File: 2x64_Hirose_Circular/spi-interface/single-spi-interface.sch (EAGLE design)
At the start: 52 parts, among them P0 BLUE, P1 BLUE, P2 BLUE, P3 BLUE, P4 BLUE, Q1 SSM3K324, Q2 SSM3J328

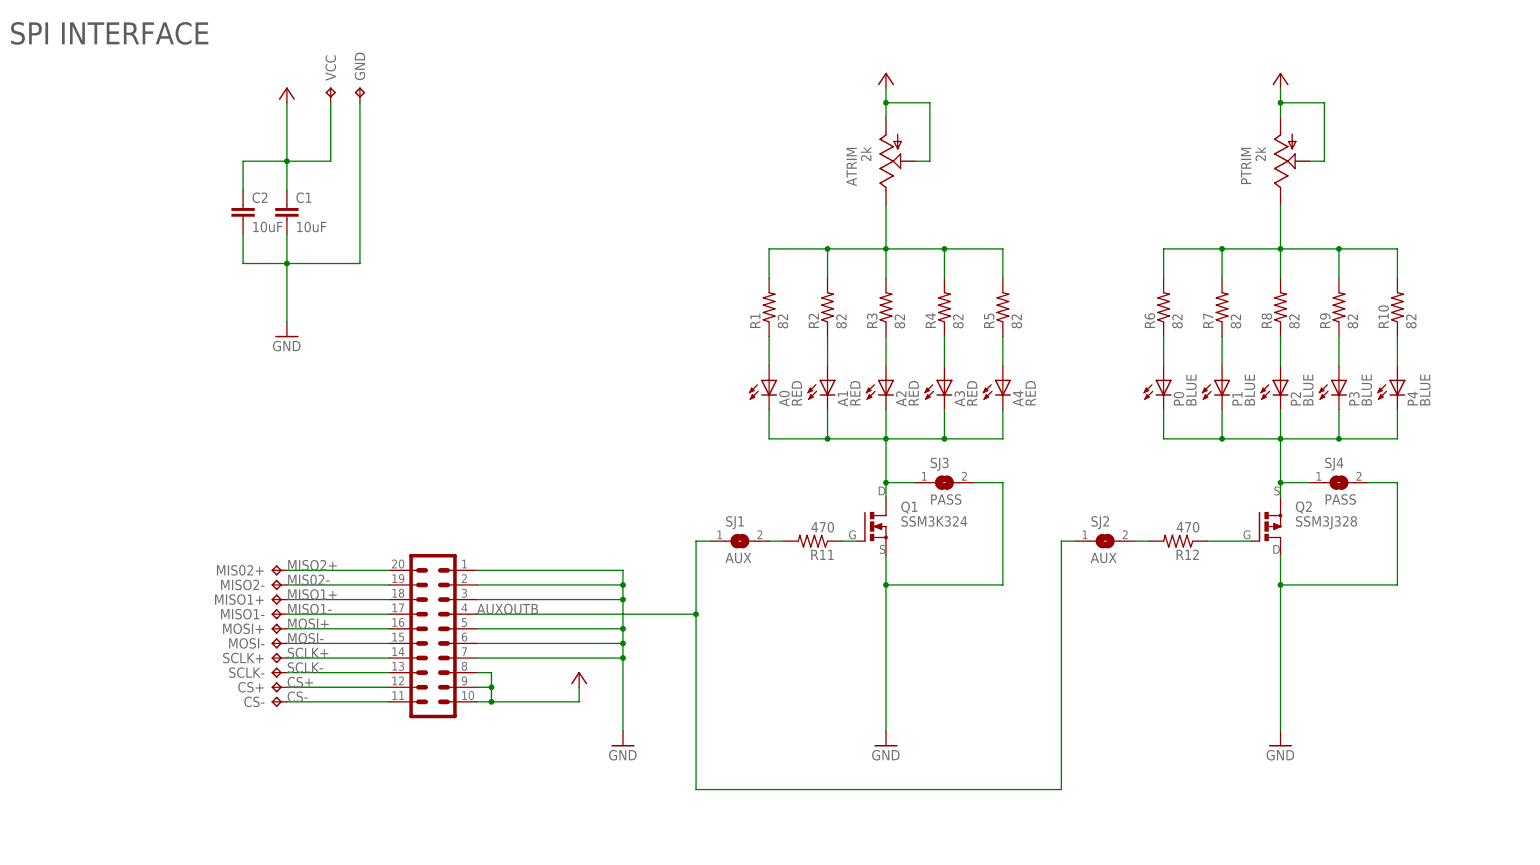
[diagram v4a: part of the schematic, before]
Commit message: Started applying revisions obtained from mechanical mockups
- This is the start of work toward rev 1.1 of Hirose 128 headstages.
- Headstages are designed to be semi-perminent. They are travel with the
  animal until it is sacraficed.
- Major changes to SPI interface board to get it working with Oat
  tracker and to conform with the semi-periment design decision.
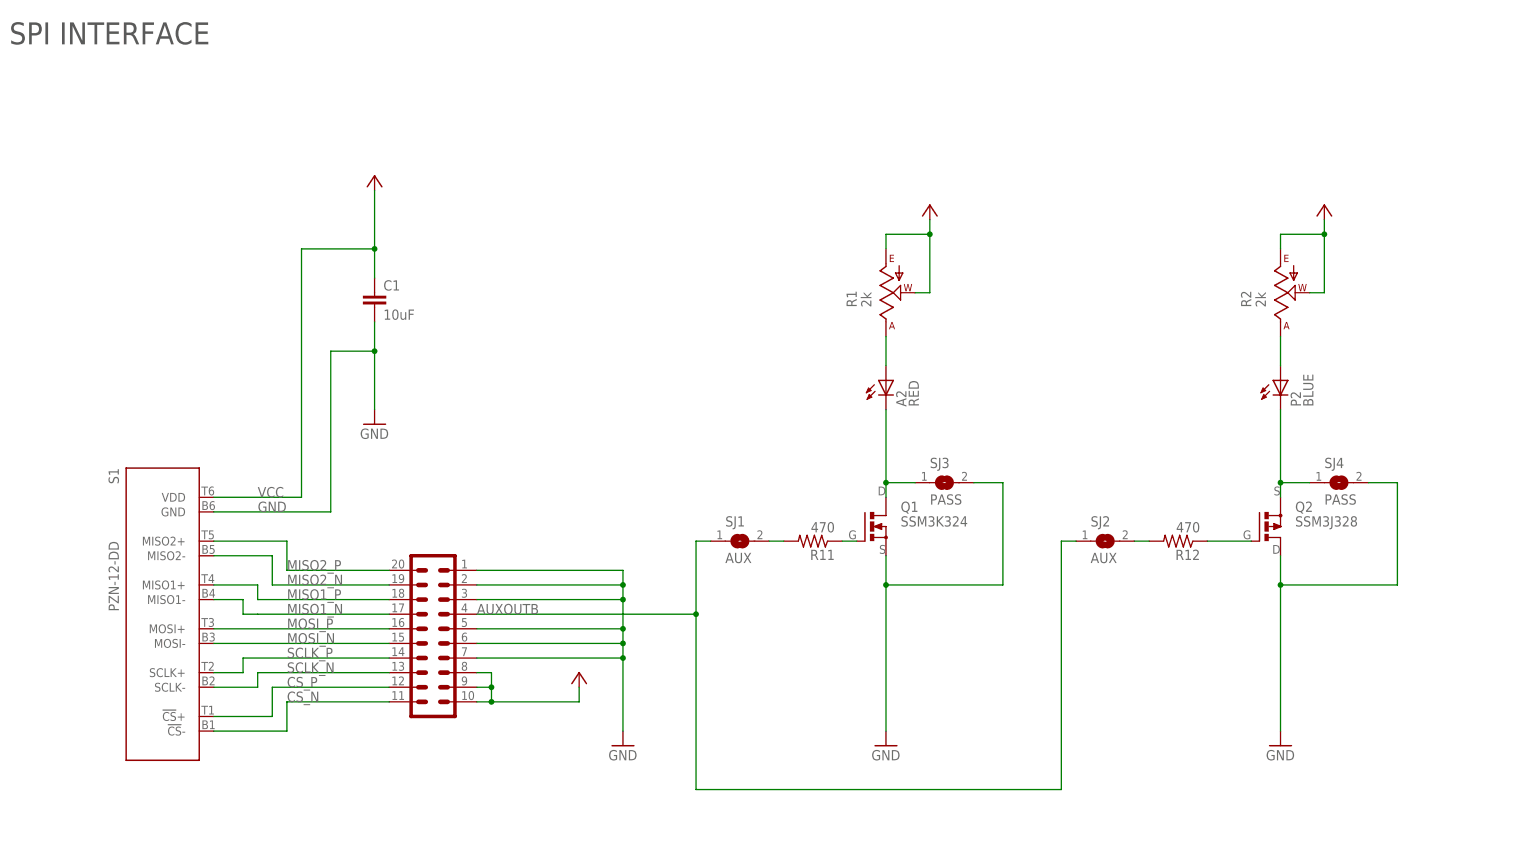
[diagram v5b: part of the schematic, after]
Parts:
- removed A0, A1, A3, A4: RED, jonnew:LED_0402
- removed ATRIM, PTRIM: 2k, headstage:TRIM_EIA/EIAJ
- removed C2: 10uF, headstage:C_0805
- removed CS+, MIS02+, MISO1+, MOSI+, SCLK+, VCC: TP_SPI_WIRE+, jonnew:TP_SPI_WIRE+
- removed CS-, GND, MISO1-, MISO2-, MOSI-, SCLK-: TP_SPI_WIRE-, jonnew:TP_SPI_WIRE-
- removed P0, P1, P3, P4: BLUE, jonnew:LED_0402
- removed R10, R3, R4, R5, R6, R7, R8, R9: 82, jonnew:R_0402
- added S1: PZN-12-DD, jonnew:RHD2000-CABLE-AMP-SIDE_PZN-12-DD
- A2, P2: device jonnew:LED_0402 -> jonnew:LED_MLE
- R1, R2: value 82 -> 2k; device jonnew:R_0402 -> jonnew:TRIM_US-SM-42/43W
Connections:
- removed net CS+: CS+.TP, DIO_E1B.12
- removed net CS-: CS-.TP, DIO_E1B.11
- removed net MIS02-: DIO_E1B.19, MISO2-.TP
- removed net MISO1+: DIO_E1B.18, MISO1+.TP
- removed net MISO1-: DIO_E1B.17, MISO1-.TP
- removed net MISO2+: DIO_E1B.20, MIS02+.TP
- removed net MOSI+: DIO_E1B.16, MOSI+.TP
- removed net MOSI-: DIO_E1B.15, MOSI-.TP
- removed net N$1: ATRIM.E, R1.2, R2.2, R3.2, R4.2, R5.2
- removed net N$10: A3.A, R4.1
- removed net N$11: P3.A, R9.1
- removed net N$12: P1.A, R7.1
- removed net N$14: A4.A, R5.1
- removed net N$15: P4.A, R10.1
- removed net N$2: P0.A, R6.1
- removed net N$3: A0.A, R1.1
- removed net N$6: PTRIM.E, R10.2, R6.2, R7.2, R8.2, R9.2
- removed net N$8: A1.A, R2.1
- removed net SCLK+: DIO_E1B.14, SCLK+.TP
- removed net SCLK-: DIO_E1B.13, SCLK-.TP
- new net CS_N: DIO_E1B.11, S1.!CS!-
- new net CS_P: DIO_E1B.12, S1.!CS!+
- new net MISO1_N: DIO_E1B.17, S1.MISO1-
- new net MISO1_P: DIO_E1B.18, S1.MISO1+
- new net MISO2_N: DIO_E1B.19, S1.MISO2-
- new net MISO2_P: DIO_E1B.20, S1.MISO2+
- new net MOSI_N: DIO_E1B.15, S1.MOSI-
- new net MOSI_P: DIO_E1B.16, S1.MOSI+
- new net SCLK_N: DIO_E1B.13, S1.SCLK-
- new net SCLK_P: DIO_E1B.14, S1.SCLK+
- net B2: no longer P0.C, P1.C, P3.C, P4.C
- net F1: no longer A0.C, A1.C, A3.C, A4.C
- net GND: now also S1.GND; no longer C2.2, GND.TP
- net N$13: now also R2.A; no longer R8.1
- net N$9: now also R1.A; no longer R3.1
- net VCC: now also R1.E, R1.W, R2.E, R2.W, S1.VDD; no longer ATRIM.A, ATRIM.S, C2.1, PTRIM.A, PTRIM.S, VCC.TP
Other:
- moved on the sheet: C1

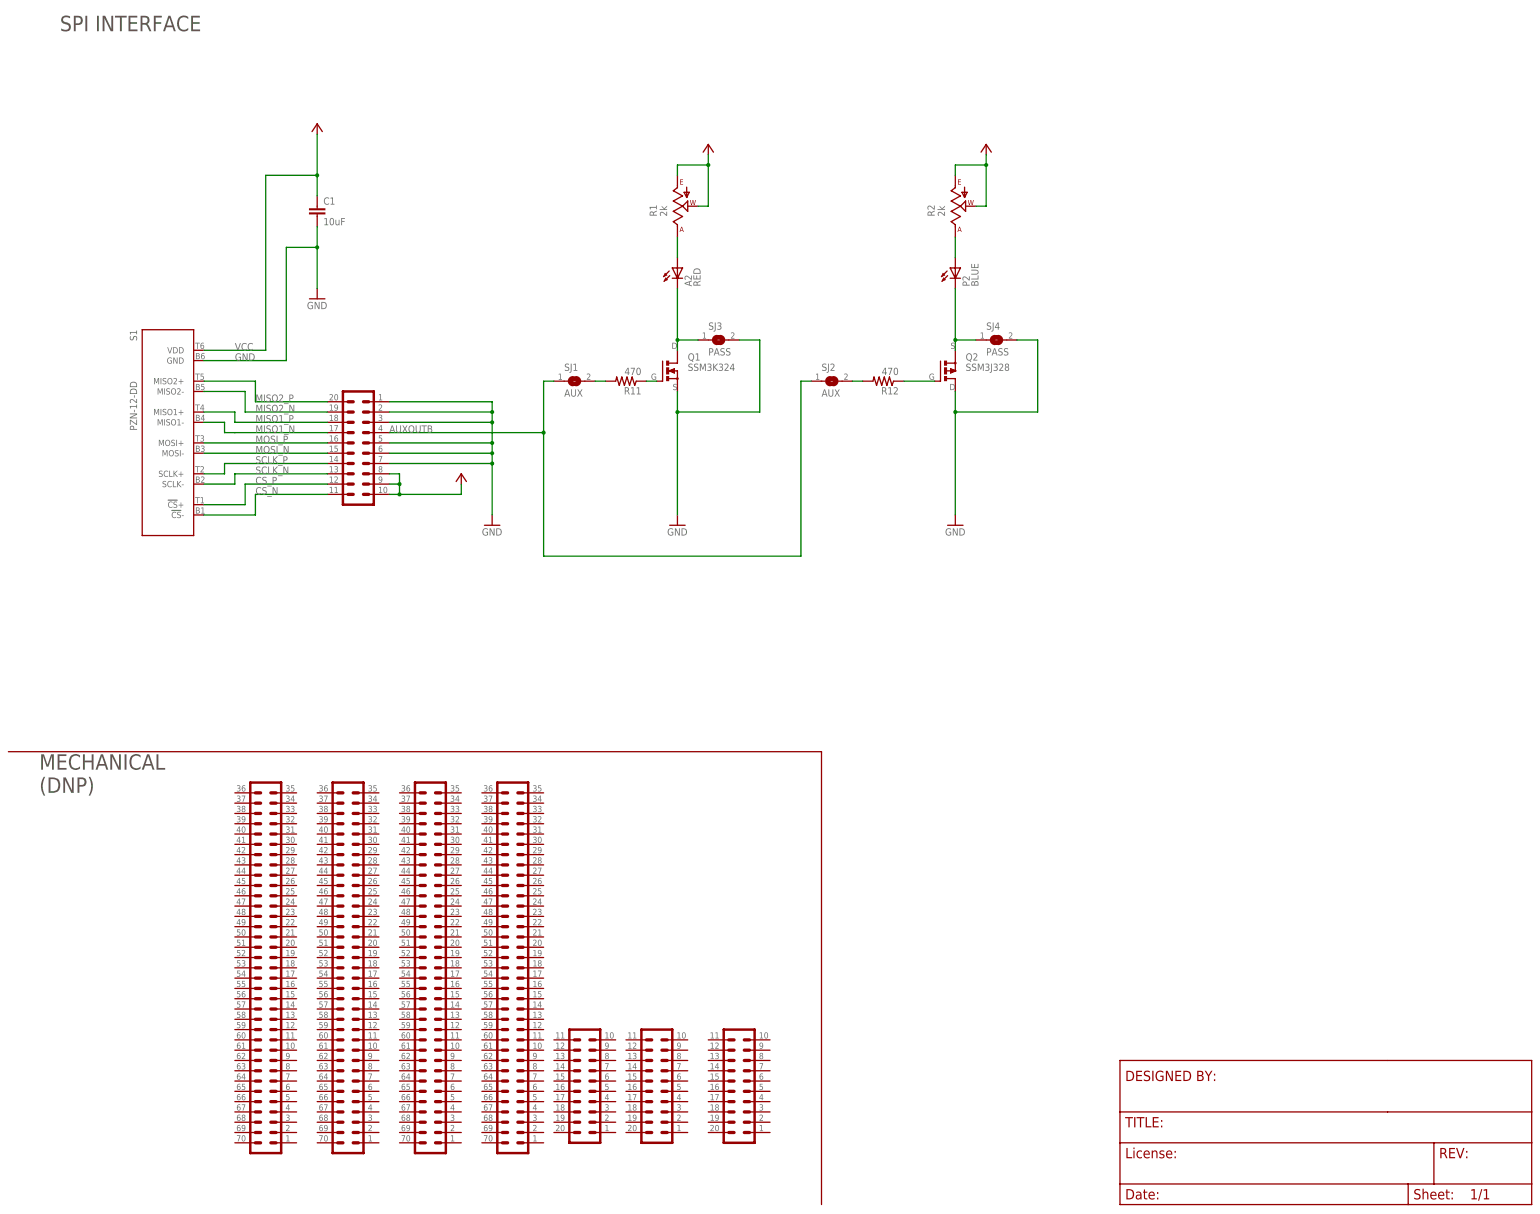
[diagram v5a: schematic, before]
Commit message: Nearly finished with revision 1.1 of Hirose-128 headstage.
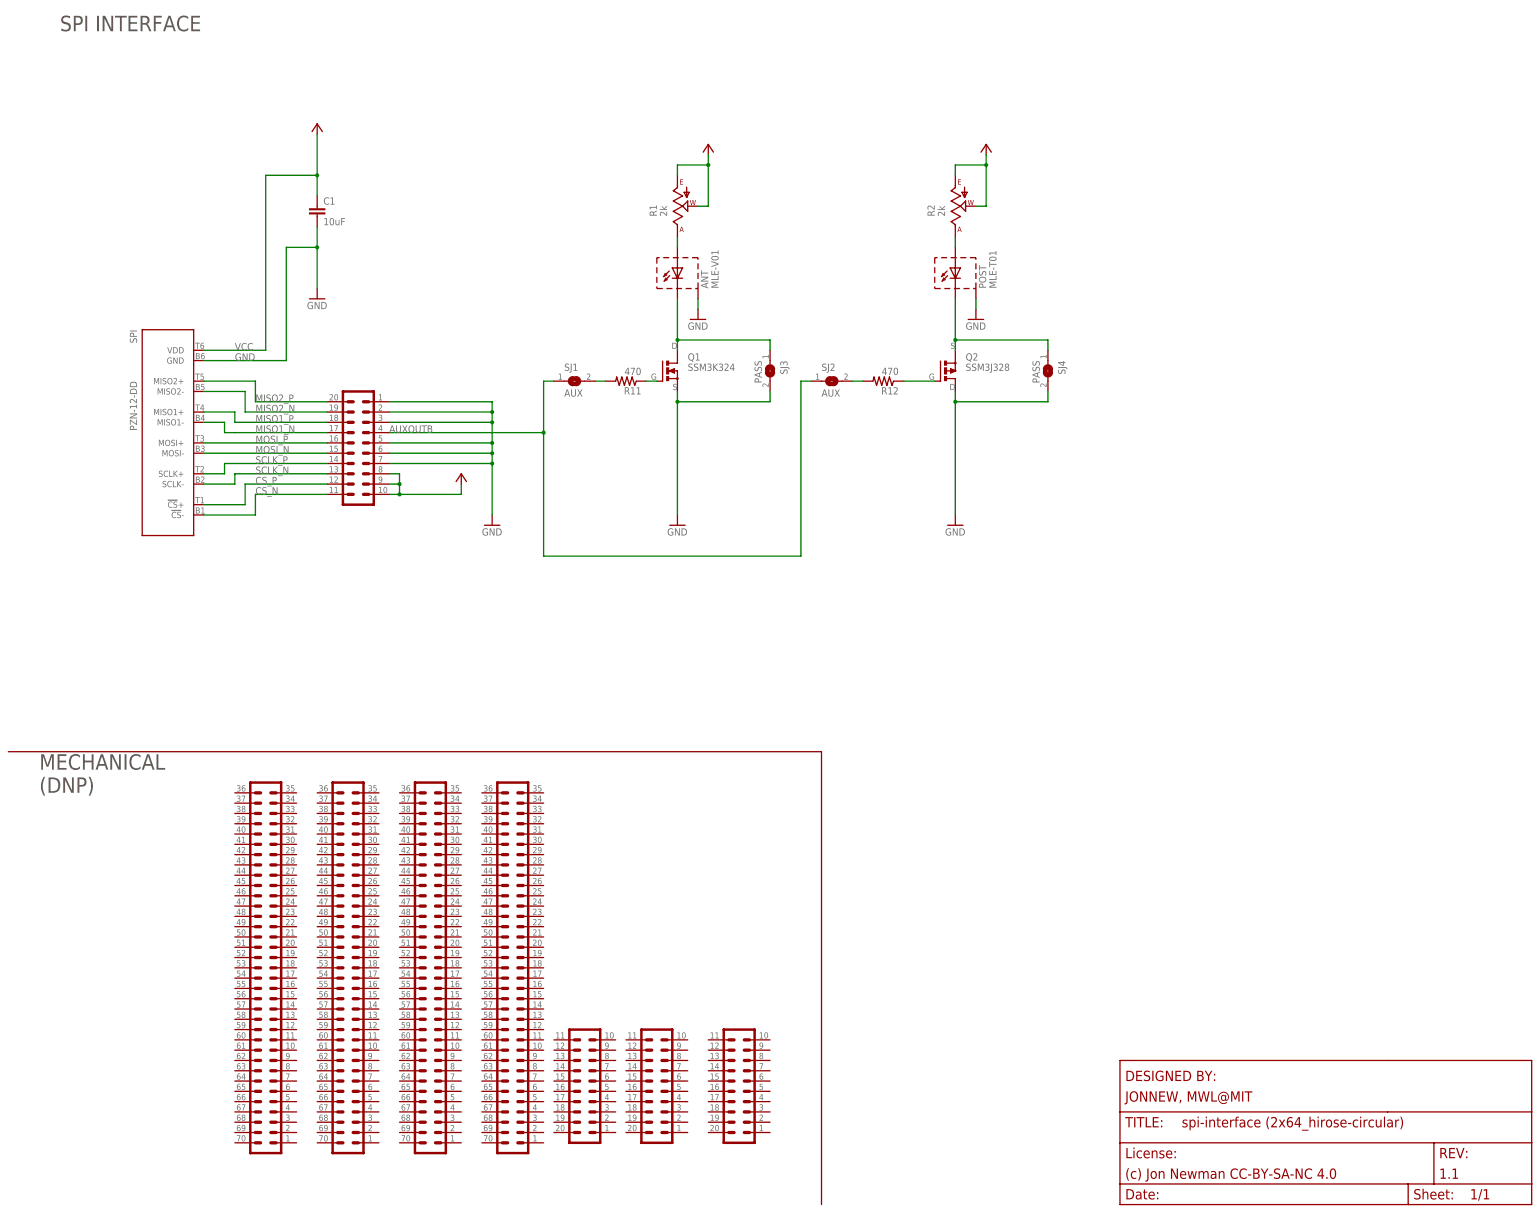
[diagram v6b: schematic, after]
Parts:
- removed A2: RED, jonnew:LED_MLE
- removed P2: BLUE, jonnew:LED_MLE
- added ANT: MLE-V01, jonnew:LED_PKG-BODY
- added POST: MLE-T01, jonnew:LED_PKG-BODY
- renumbered S1 to SPI
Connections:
- net B2: now also POST.C; no longer P2.C
- net F1: now also ANT.C; no longer A2.C
- net GND: now also ANT.BODY, POST.BODY
- net N$13: now also POST.A; no longer P2.A
- net N$9: now also ANT.A; no longer A2.A
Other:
- moved on the sheet: SJ3, SJ4

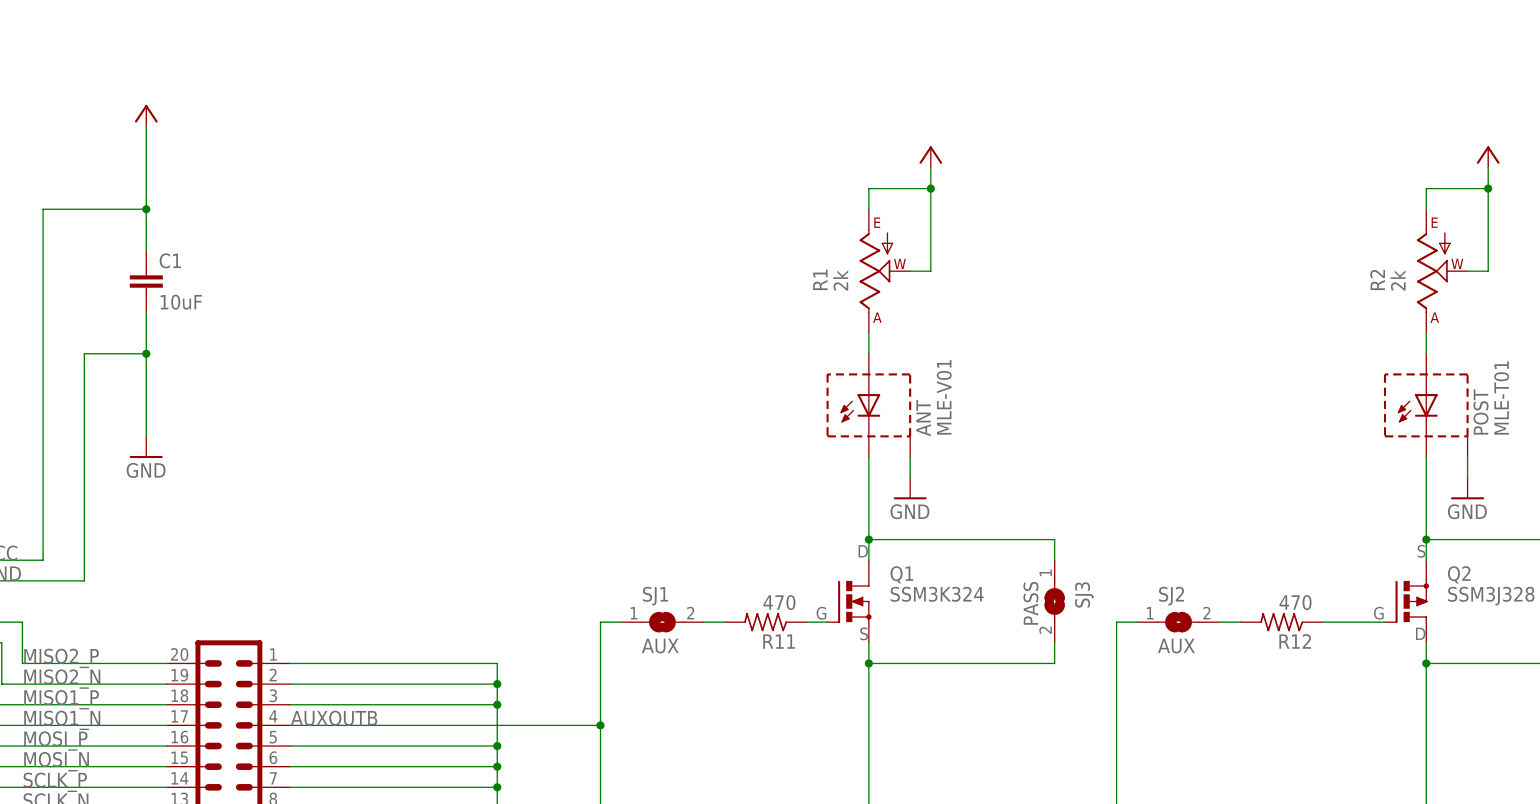
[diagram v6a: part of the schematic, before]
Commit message: Handled most of the remaining TODOs
- Ordered functional version of the eib and spi interface boards from
  OSH park.
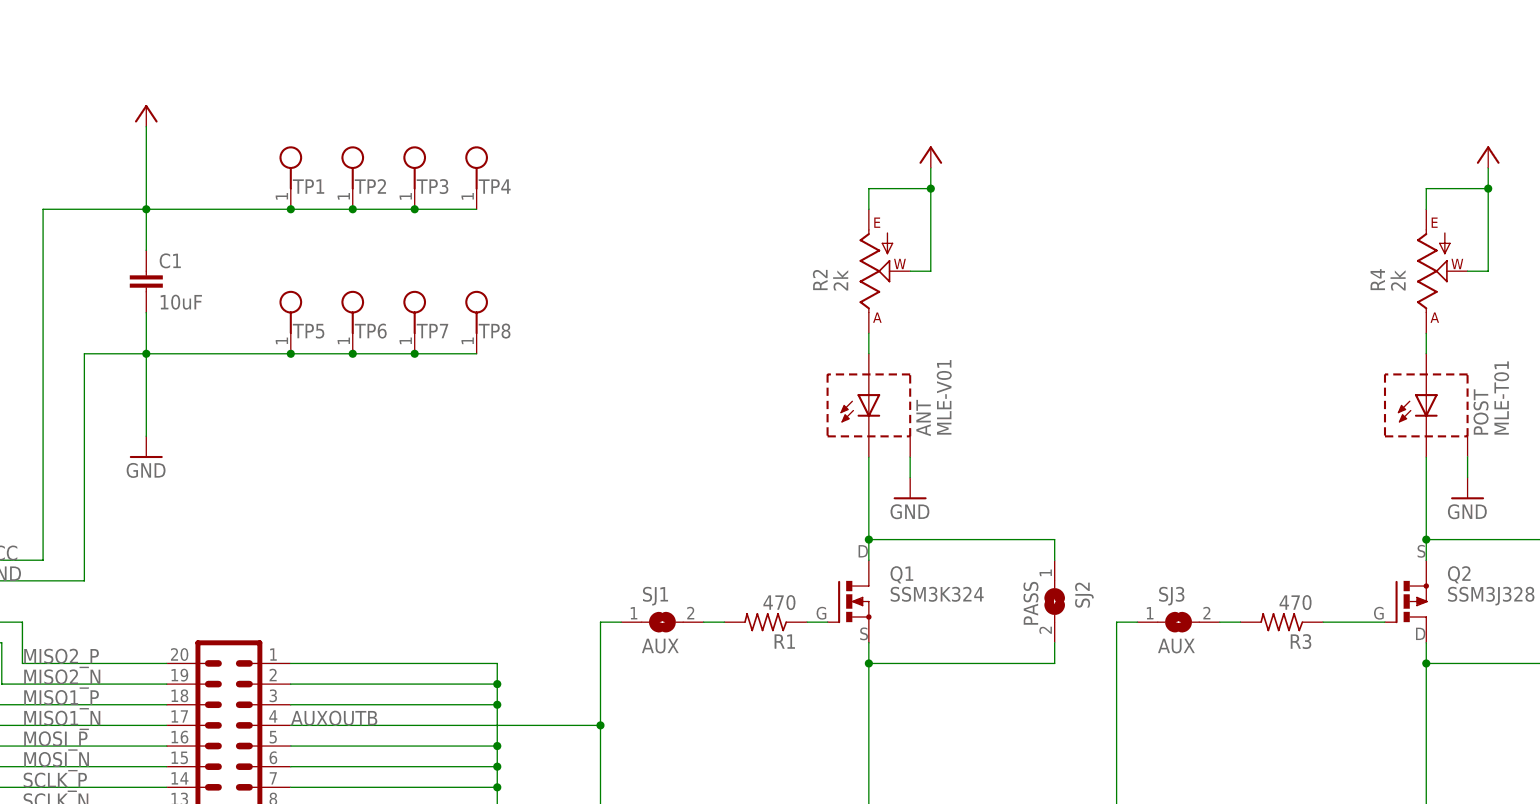
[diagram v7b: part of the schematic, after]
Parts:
- removed R11, R12: 470, headstage:R_0402
- added R3: 470, jonnew:R_0603
- added R4: 2k, jonnew:TRIM_US-SM-42/43W
- added TP1, TP2, TP3, TP4, TP5, TP6, TP7, TP8: (no value), jonnew:TESTPOINT_SMALL
- R1: value 2k -> 470; device jonnew:TRIM_US-SM-42/43W -> jonnew:R_0603
- SJ2: value AUX -> PASS
- SJ3: value PASS -> AUX
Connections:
- net AUXOUTB: now also SJ3.1; no longer SJ2.1
- net F1: now also SJ2.1; no longer SJ3.1
- net GND: now also SJ2.2, TP5.1, TP6.1, TP7.1, TP8.1; no longer SJ3.2
- net N$13: now also R4.A; no longer R2.A
- net N$28: now also R1.1; no longer R11.1
- net N$34: now also R1.2; no longer R11.2
- net N$4: now also R3.2, SJ3.2; no longer R12.2, SJ2.2
- net N$5: now also R3.1; no longer R12.1
- net N$9: now also R2.A; no longer R1.A
- net VCC: now also R4.E, R4.W, TP1.1, TP2.1, TP3.1, TP4.1; no longer R1.E, R1.W
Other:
- moved on the sheet: R2, SJ2, SJ3
